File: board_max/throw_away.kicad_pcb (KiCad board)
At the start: 2 copper layers, 6 parts, among them U1 MAX4820xUP, U2 MAX4820xUP, U3 MAX4820xUP, U4 MAX4820xUP, U5 MAX4820xUP, U6 ESP32-S3-DevKitC

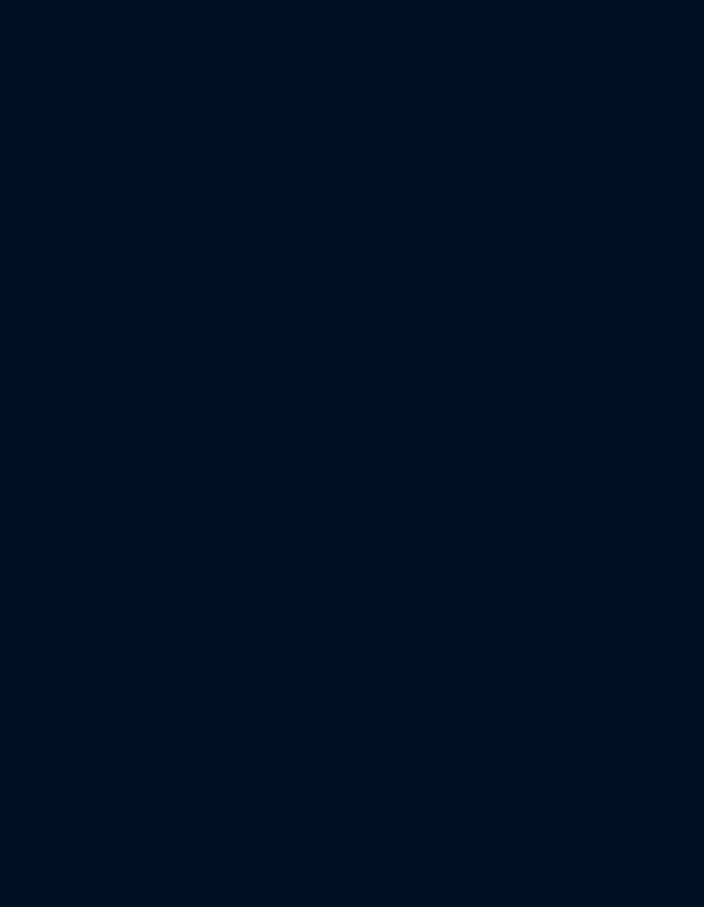
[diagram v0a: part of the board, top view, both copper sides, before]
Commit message: finished connecting max4820 chips to ESP32
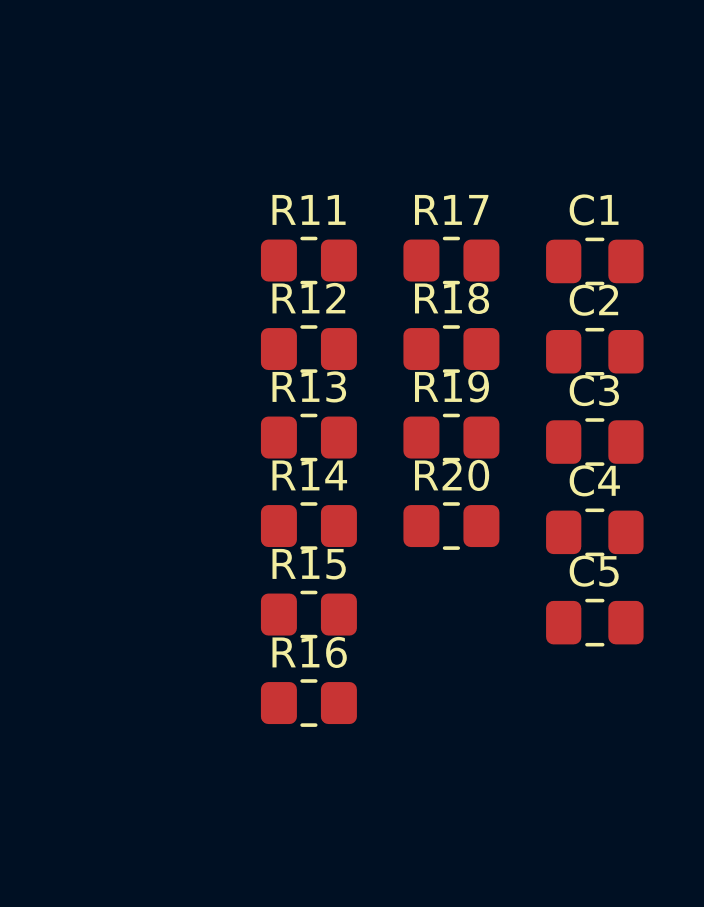
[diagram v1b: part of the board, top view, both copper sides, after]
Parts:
- added C1: 0.1uf, Capacitor_SMD:C_0805_2012Metric_Pad1.18x1.45mm_HandSolder, F.Cu at (126.0, 67.0)
- added C2: 0.1uf, Capacitor_SMD:C_0805_2012Metric_Pad1.18x1.45mm_HandSolder, F.Cu at (126.0, 70.0)
- added C3: 0.1uf, Capacitor_SMD:C_0805_2012Metric_Pad1.18x1.45mm_HandSolder, F.Cu at (126.0, 73.0)
- added C4: 0.1uf, Capacitor_SMD:C_0805_2012Metric_Pad1.18x1.45mm_HandSolder, F.Cu at (126.0, 76.0)
- added C5: 0.1uf, Capacitor_SMD:C_0805_2012Metric_Pad1.18x1.45mm_HandSolder, F.Cu at (126.0, 79.0)
- added R11: 10K, Resistor_SMD:R_0805_2012Metric_Pad1.20x1.40mm_HandSolder, F.Cu at (116.4, 66.9)
- added R12: 10K, Resistor_SMD:R_0805_2012Metric_Pad1.20x1.40mm_HandSolder, F.Cu at (116.4, 69.9)
- added R13: 10K, Resistor_SMD:R_0805_2012Metric_Pad1.20x1.40mm_HandSolder, F.Cu at (116.4, 72.8)
- added R14: 10K, Resistor_SMD:R_0805_2012Metric_Pad1.20x1.40mm_HandSolder, F.Cu at (116.4, 75.8)
- added R15: 10K, Resistor_SMD:R_0805_2012Metric_Pad1.20x1.40mm_HandSolder, F.Cu at (116.4, 78.7)
- added R16: 10K, Resistor_SMD:R_0805_2012Metric_Pad1.20x1.40mm_HandSolder, F.Cu at (116.4, 81.7)
- added R17: 10K, Resistor_SMD:R_0805_2012Metric_Pad1.20x1.40mm_HandSolder, F.Cu at (121.2, 66.9)
- added R18: 10K, Resistor_SMD:R_0805_2012Metric_Pad1.20x1.40mm_HandSolder, F.Cu at (121.2, 69.9)
- added R19: 10K, Resistor_SMD:R_0805_2012Metric_Pad1.20x1.40mm_HandSolder, F.Cu at (121.2, 72.8)
- added R20: 10K, Resistor_SMD:R_0805_2012Metric_Pad1.20x1.40mm_HandSolder, F.Cu at (121.2, 75.8)
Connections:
- U1 pad 2: unconnected-(U1-~{SET}-Pad2) -> PU10
- U1 pad 3: unconnected-(U1-~{RESET}-Pad3) -> PU1
- U1 pad 4: unconnected-(U1-~{CS}-Pad4) -> Net-(U1-~{CS})
- U1 pad 5: unconnected-(U1-DIN-Pad5) -> MOSI
- U1 pad 6: unconnected-(U1-SCLK-Pad6) -> SCLK
- U2 pad 2: unconnected-(U2-~{SET}-Pad2) -> PU10
- U2 pad 3: unconnected-(U2-~{RESET}-Pad3) -> PU1
- U2 pad 4: unconnected-(U2-~{CS}-Pad4) -> Net-(U2-~{CS})
- U2 pad 5: unconnected-(U2-DIN-Pad5) -> MOSI
- U2 pad 6: unconnected-(U2-SCLK-Pad6) -> SCLK
- U3 pad 2: unconnected-(U3-~{SET}-Pad2) -> PU10
- U3 pad 3: unconnected-(U3-~{RESET}-Pad3) -> PU1
- U3 pad 4: unconnected-(U3-~{CS}-Pad4) -> Net-(U3-~{CS})
- U3 pad 5: unconnected-(U3-DIN-Pad5) -> MOSI
- U3 pad 6: unconnected-(U3-SCLK-Pad6) -> SCLK
- U4 pad 2: unconnected-(U4-~{SET}-Pad2) -> PU10
- U4 pad 3: unconnected-(U4-~{RESET}-Pad3) -> PU1
- U4 pad 4: unconnected-(U4-~{CS}-Pad4) -> Net-(U4-~{CS})
- U4 pad 5: unconnected-(U4-DIN-Pad5) -> MOSI
- U4 pad 6: unconnected-(U4-SCLK-Pad6) -> SCLK
- U5 pad 2: unconnected-(U5-~{SET}-Pad2) -> PU10
- U5 pad 3: unconnected-(U5-~{RESET}-Pad3) -> PU1
- U5 pad 4: unconnected-(U5-~{CS}-Pad4) -> Net-(U5-~{CS})
- U5 pad 5: unconnected-(U5-DIN-Pad5) -> MOSI
- U5 pad 6: unconnected-(U5-SCLK-Pad6) -> SCLK
- U6 pad 16: unconnected-(U6-GPIO10/ADC1_CH9-Pad16) -> Net-(U1-~{CS})
- U6 pad 17: unconnected-(U6-GPIO11/ADC2_CH0-Pad17) -> MOSI
- U6 pad 18: unconnected-(U6-GPIO12/ADC2_CH1-Pad18) -> SCLK
- U6 pad 19: unconnected-(U6-GPIO13/ADC2_CH2-Pad19) -> Net-(U2-~{CS})
- U6 pad 20: unconnected-(U6-GPIO14/ADC2_CH3-Pad20) -> Net-(U3-~{CS})
- U6 pad 27: unconnected-(U6-GPIO21-Pad27) -> Net-(U4-~{CS})
- U6 pad 39: unconnected-(U6-GPIO42/MTMS-Pad39) -> PU1
- U6 pad 40: unconnected-(U6-GPIO2/ADC1_CH1-Pad40) -> PU10
- U6 pad 41: unconnected-(U6-GPIO1/ADC1_CH0-Pad41) -> Net-(U5-~{CS})

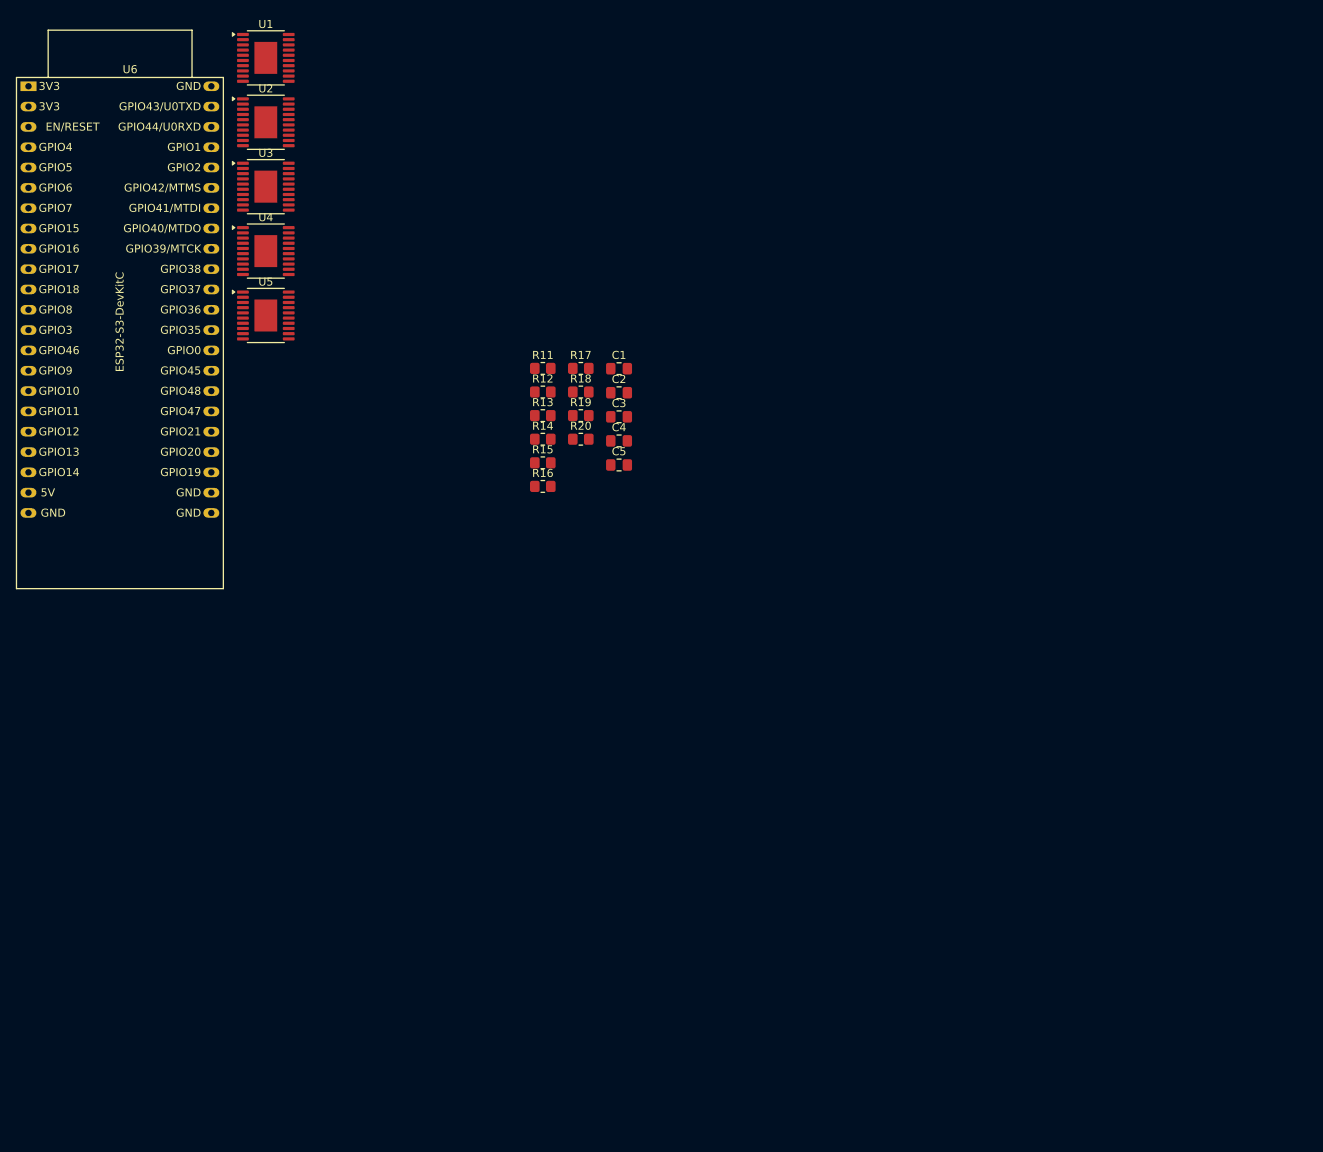
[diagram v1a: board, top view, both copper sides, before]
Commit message: We added dual operating mode support to the GAP Tuner: Field mode (AP) is now a first-class operating mode stored in NVS flash alongside Home WiFi mode, with NetworkMgr refactored to drop   its own web server and WebServerManager taking sole ownership of all HTTP routing in both modes. A gear icon on the main tuner page links to a new /settings page where the user can toggle   between modes — displaying AP credentials in field mode and a pre-populated WiFi credential form in home mode — with the Apply & Restart button disabled until something actually changes,   context-sensitive status copy ("X mode is active" vs "Switch to X mode"), and post-save instructions that include a 20-second countdown redirect to gaptuner.local when switching to home   mode, using an AbortController timeout to ensure the instructions appear even when the device restarts before the HTTP response is delivered.
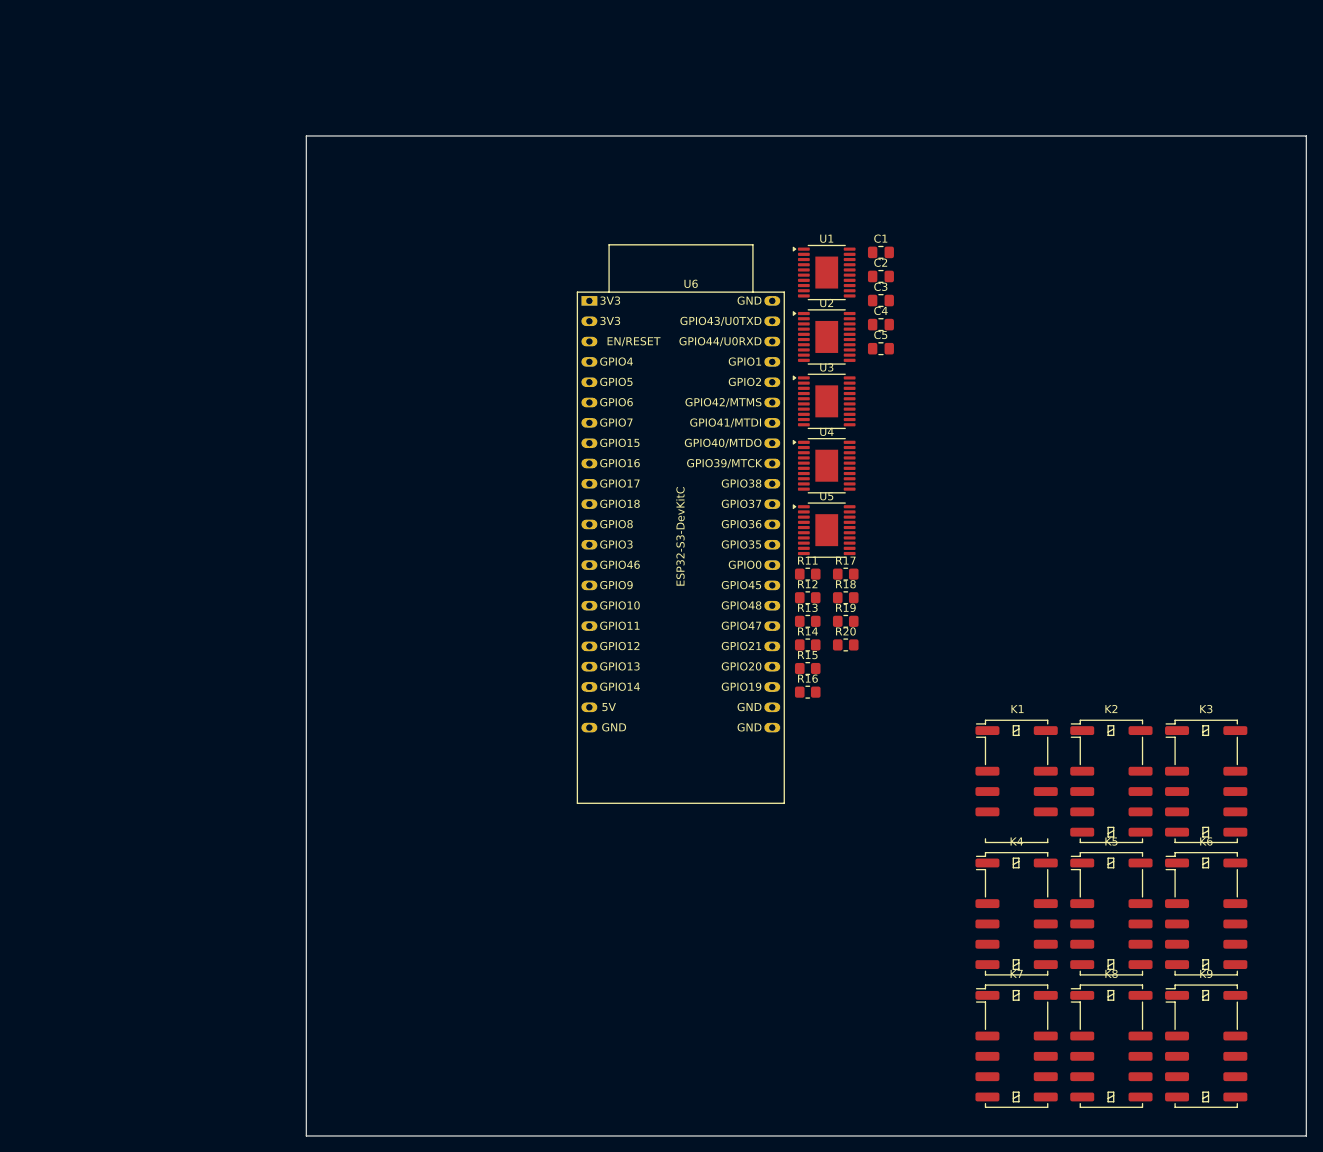
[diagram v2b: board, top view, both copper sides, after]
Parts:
- added K1: EE2-3NU, Relay_SMD:Relay_DPDT_Kemet_EE2_NU, F.Cu at (175.7, 118.5)
- added K2: EE2-3TNU, Relay_SMD:Relay_DPDT_Kemet_EE2_NU_DoubleCoil, F.Cu at (187.5, 118.5)
- added K3: EE2-3TNU, Relay_SMD:Relay_DPDT_Kemet_EE2_NU_DoubleCoil, F.Cu at (199.4, 118.5)
- added K4: EE2-3TNU, Relay_SMD:Relay_DPDT_Kemet_EE2_NU_DoubleCoil, F.Cu at (175.7, 135.1)
- added K5: EE2-3TNU, Relay_SMD:Relay_DPDT_Kemet_EE2_NU_DoubleCoil, F.Cu at (187.5, 135.1)
- added K6: EE2-3TNU, Relay_SMD:Relay_DPDT_Kemet_EE2_NU_DoubleCoil, F.Cu at (199.4, 135.1)
- added K7: EE2-3TNU, Relay_SMD:Relay_DPDT_Kemet_EE2_NU_DoubleCoil, F.Cu at (175.7, 151.7)
- added K8: EE2-3TNU, Relay_SMD:Relay_DPDT_Kemet_EE2_NU_DoubleCoil, F.Cu at (187.5, 151.7)
- added K9: EE2-3TNU, Relay_SMD:Relay_DPDT_Kemet_EE2_NU_DoubleCoil, F.Cu at (199.4, 151.7)
- moved U1 75.1 mm to (151.9, 54.9)
- moved U2 75.1 mm to (151.9, 63.0)
- moved U3 75.1 mm to (151.9, 71.0)
- moved U4 75.1 mm to (151.9, 79.1)
- moved U6 75.1 mm to (122.3, 58.5)
- moved U5 75.1 mm to (151.9, 87.1)
- moved R11 41.9 mm to (149.5, 92.6)
- moved R12 41.9 mm to (149.5, 95.6)
- moved R13 41.9 mm to (149.5, 98.5)
- moved R14 41.9 mm to (149.5, 101.5)
- moved R15 41.9 mm to (149.5, 104.4)
- moved R16 41.9 mm to (149.5, 107.4)
- moved R17 41.9 mm to (154.3, 92.6)
- moved R18 41.9 mm to (154.3, 95.6)
- moved R19 41.9 mm to (154.3, 98.5)
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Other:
- board outline added: 125 x 125 mm
